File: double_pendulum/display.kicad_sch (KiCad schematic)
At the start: 1 part, among them J3 1734839-8

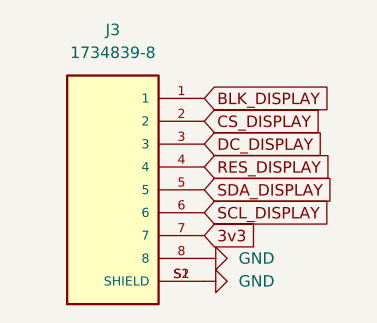
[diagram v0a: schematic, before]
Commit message: Finished schematic and layout of the double pendulum
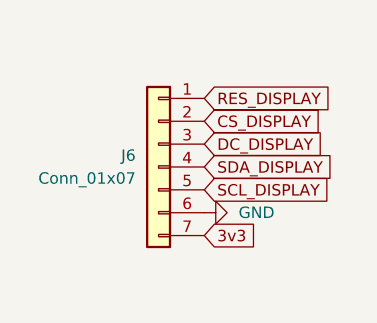
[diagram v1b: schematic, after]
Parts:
- removed J3: 1734839-8, 1734839_8:TE_1734839-8, symbol 1734839_8:1734839-8
- added J6: Conn_01x07, Connector_JST:JST_VH_B7P-VH_1x07_P3.96mm_Vertical, symbol Connector_Generic:Conn_01x07
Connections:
- net 3v3: now also J6.7 (Pin_7)
- net CS_DISPLAY: now also J6.2 (Pin_2)
- net DC_DISPLAY: now also J6.3 (Pin_3)
- net GND: now also J6.6 (Pin_6)
- net RES_DISPLAY: now also J6.1 (Pin_1)
- net SCL_DISPLAY: now also J6.5 (Pin_5)
- net SDA_DISPLAY: now also J6.4 (Pin_4)
